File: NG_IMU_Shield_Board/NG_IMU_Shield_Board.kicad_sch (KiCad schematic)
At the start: 22 parts, among them J1 Conn_01x04_Female, J2 Conn_01x02_Male, J3 Conn_01x10_Female, J4 Conn_01x03_Female, J5 Conn_02x12_Top_Bottom, J6 Conn_01x11_Male, U1 SN75ALS175, U2 Level_Converter, U3 Teensy_v4.0

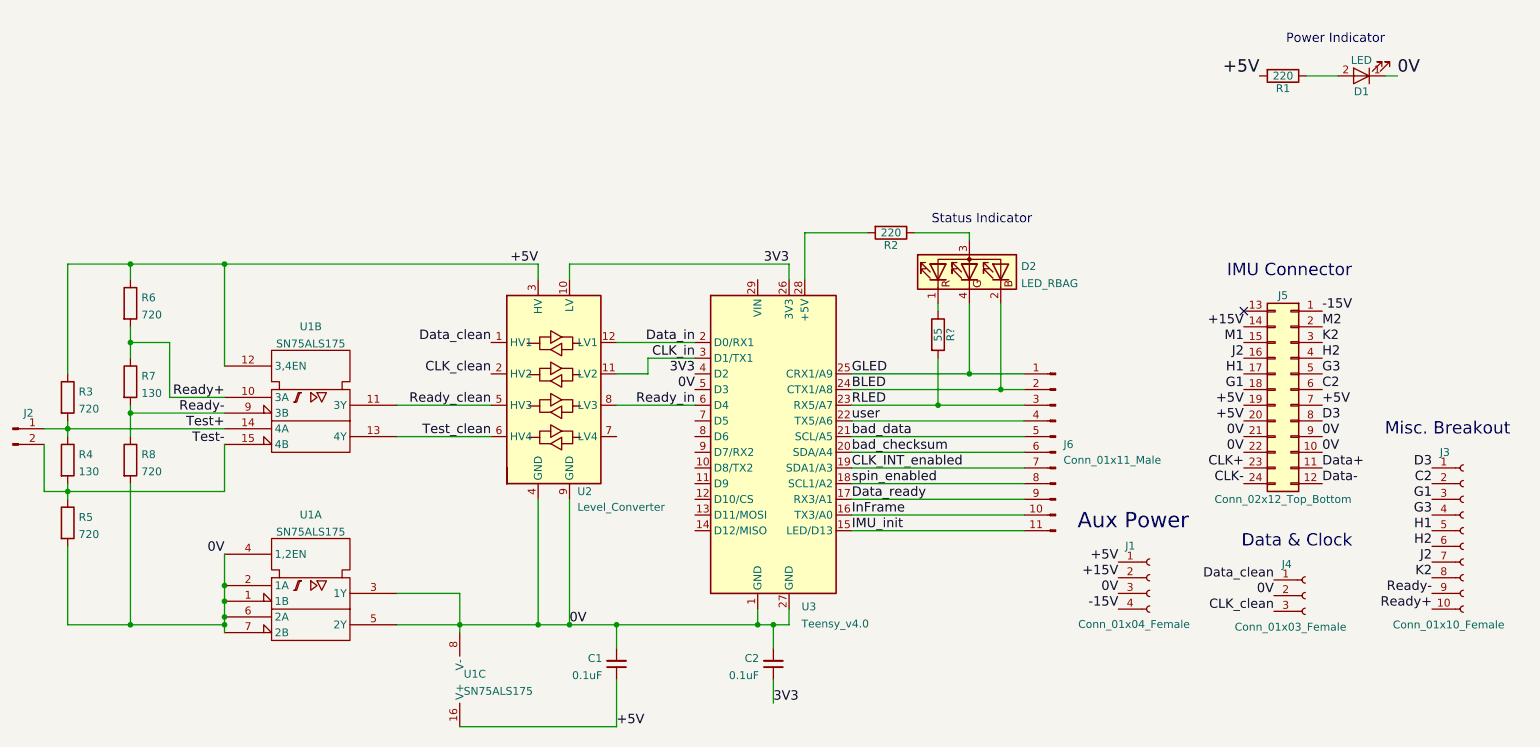
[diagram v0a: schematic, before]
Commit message: Simplified and updated footprints to ease routing
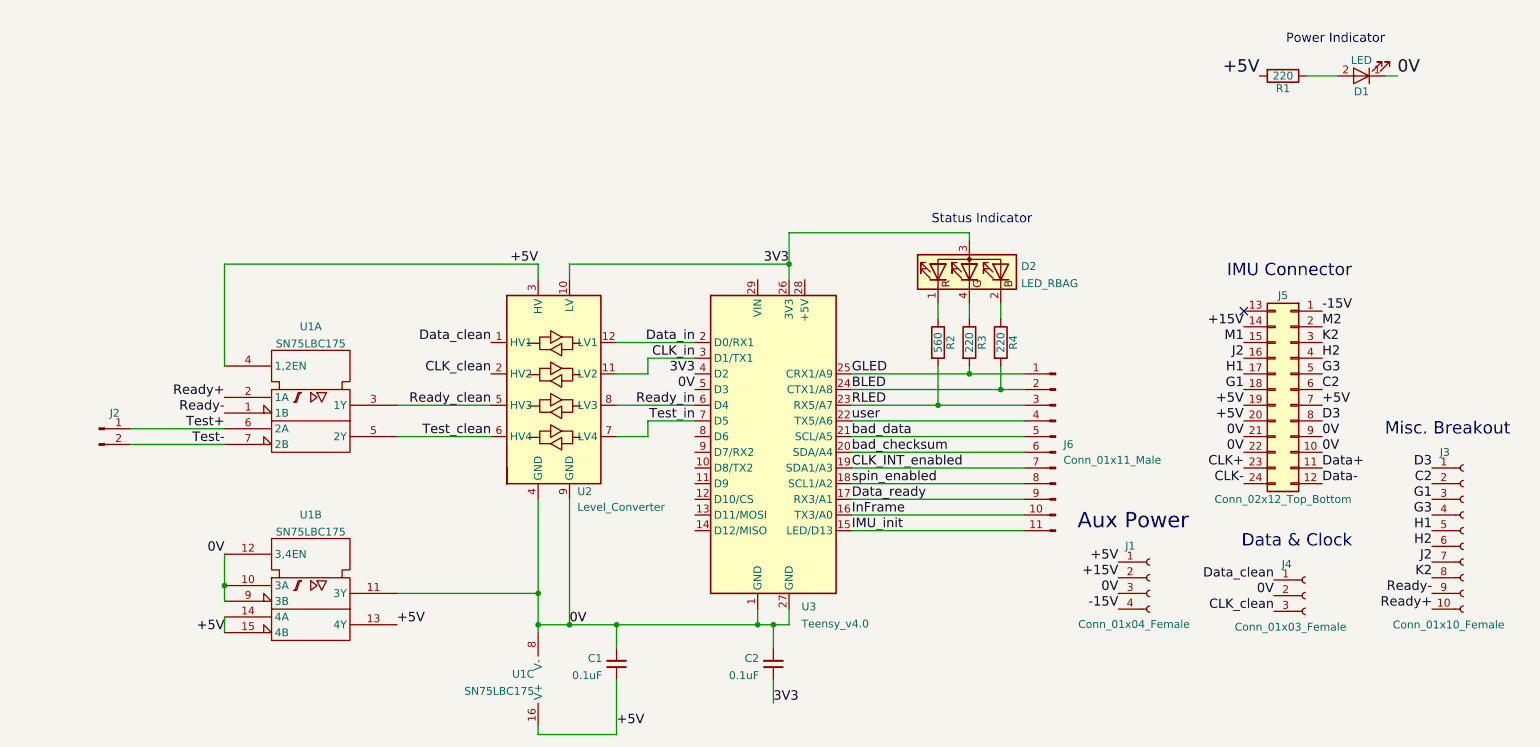
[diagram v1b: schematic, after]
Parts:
- removed R2: 220, Resistor_THT:R_Axial_DIN0204_L3.6mm_D1.6mm_P7.62mm_Horizontal, symbol NG_IMU_Interface_Board-rescue:R
- removed R3, R5, R6, R8: 720, Resistor_THT:R_Axial_DIN0204_L3.6mm_D1.6mm_P7.62mm_Horizontal, symbol Device:R
- removed R4, R7: 130, Resistor_THT:R_Axial_DIN0204_L3.6mm_D1.6mm_P7.62mm_Horizontal, symbol Device:R
- added R3, R4: 220, Resistor_SMD:R_0805_2012Metric_Pad1.20x1.40mm_HandSolder, symbol NG_IMU_Interface_Board-rescue:R
- R1: footprint Resistor_THT:R_Axial_DIN0204_L3.6mm_D1.6mm_P7.62mm_Horizontal -> Resistor_SMD:R_0805_2012Metric_Pad1.20x1.40mm_HandSolder
- R2: renamed from R?; value 55 -> 560; footprint Resistor_THT:R_Axial_DIN0204_L3.6mm_D1.6mm_P7.62mm_Horizontal -> Resistor_SMD:R_0805_2012Metric_Pad1.20x1.40mm_HandSolder
- U1: value SN75ALS175 -> SN75LBC175; footprint Package_DIP:DIP-16_W7.62mm_Socket -> Package_SO:SOIC-16_3.9x9.9mm_P1.27mm
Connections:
- net +5V: now also U1.13 (4Y), U1.14 (4A), U1.15 (4B), U1.4 (1,2EN); no longer U1.12 (3,4EN)
- net 0V: now also U1.10 (3A), U1.11 (3Y), U1.12 (3,4EN), U1.9 (3B); no longer U1.1 (1B), U1.2 (1A), U1.3 (1Y), U1.4 (1,2EN), U1.5 (2Y), U1.6 (2A), U1.7 (2B)
- net 3V3: now also D2.3 (A)
- net BLED: now also R4.2; no longer D2.2 (BK)
- net GLED: now also R3.2; no longer D2.4 (GK)
- net Ready+: now also U1.2 (1A); no longer U1.10 (3A)
- net Ready-: now also U1.1 (1B); no longer U1.9 (3B)
- net Ready_clean: now also U1.3 (1Y); no longer U1.11 (3Y)
- net Test+: now also U1.6 (2A); no longer U1.14 (4A)
- net Test-: now also U1.7 (2B); no longer U1.15 (4B)
- net Test_clean: now also U1.5 (2Y); no longer U1.13 (4Y)
- net Test_in: now reaches U3.7 (D5)
- net Test_in: now also U2.7 (LV4)
- new net: D2.2 (BK), R4.1
- new net: D2.4 (GK), R3.1
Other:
- moved on the sheet: J2, R2, U1A, U1B, U1C

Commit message: Finished routing board
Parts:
- added R5, R6: 120, Resistor_SMD:R_1206_3216Metric_Pad1.30x1.75mm_HandSolder, symbol NG_IMU_Interface_Board-rescue:R
- D2: value LED_RBAG -> LED_GABR; symbol Device:LED_RBAG -> Device:LED_GABR
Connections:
- net 3V3: now also D2.2 (A); no longer D2.3 (A)
- net Ready+: now also R5.2
- net Ready-: now also R5.1
- net Test+: now also R6.1
- net Test-: now also R6.2
- net at R4.1: now also D2.3 (BK); no longer D2.2 (BK)
- net at R3.1: now also D2.1 (GK); no longer D2.4 (GK)
- net at R2.1: now also D2.4 (RK); no longer D2.1 (RK)
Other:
- moved on the sheet: J2
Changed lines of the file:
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@@
   (junction (at 142.24 68.58) (diameter 0) (color 0 0 0 0)
+  )
+  (junction (at 38.1 105.41) (diameter 0) (color 0 0 0 0)
+  )
+  (junction (at 38.1 95.25) (diameter 0) (color 0 0 0 0)
   )
   (junction (at 114.3 127) (diameter 0) (color 0 0 0 0)
@@
     (stroke (width 0) (type default) (color 0 0 0 0))
   )
+  (wire (pts (xy 29.21 105.41) (xy 38.1 105.41))
+    (stroke (width 0) (type default) (color 0 0 0 0))
+  )
+  (wire (pts (xy 38.1 95.25) (xy 50.8 95.25))
+    (stroke (width 0) (type default) (color 0 0 0 0))
+  )
   (wire (pts (xy 78.74 96.52) (xy 93.98 96.52))
     (stroke (width 0) (type default) (color 0 0 0 0))
   )
+  (wire (pts (xy 29.21 97.79) (xy 29.21 105.41))
+    (stroke (width 0) (type default) (color 0 0 0 0))
+  )
+  (wire (pts (xy 22.86 97.79) (xy 29.21 97.79))
+    (stroke (width 0) (type default) (color 0 0 0 0))
+  )
   (wire (pts (xy 119.38 86.36) (xy 119.38 83.82))
     (stroke (width 0) (type default) (color 0 0 0 0))
   )
+  (wire (pts (xy 50.8 97.79) (xy 41.91 97.79))
+    (stroke (width 0) (type default) (color 0 0 0 0))
+  )
   (wire (pts (xy 226.06 38.1) (xy 231.14 38.1))
     (stroke (width 0) (type default) (color 0 0 0 0))
@@
     (stroke (width 0) (type default) (color 0 0 0 0))
   )
+  (wire (pts (xy 41.91 82.55) (xy 38.1 82.55))
+    (stroke (width 0) (type default) (color 0 0 0 0))
+  )
   (wire (pts (xy 139.7 127) (xy 142.24 127))
     (stroke (width 0) (type default) (color 0 0 0 0))
@@
     (stroke (width 0) (type default) (color 0 0 0 0))
   )
+  (wire (pts (xy 38.1 92.71) (xy 50.8 92.71))
+    (stroke (width 0) (type default) (color 0 0 0 0))
+  )
   (wire (pts (xy 101.6 144.78) (xy 101.6 143.51))
     (stroke (width 0) (type default) (color 0 0 0 0))
@@
     (stroke (width 0) (type default) (color 0 0 0 0))
   )
+  (wire (pts (xy 38.1 91.44) (xy 38.1 92.71))
+    (stroke (width 0) (type default) (color 0 0 0 0))
+  )
   (wire (pts (xy 176.53 74.93) (xy 176.53 77.47))
     (stroke (width 0) (type default) (color 0 0 0 0))
   )
+  (wire (pts (xy 38.1 82.55) (xy 38.1 83.82))
+    (stroke (width 0) (type default) (color 0 0 0 0))
+  )
   (wire (pts (xy 114.3 130.81) (xy 114.3 127))
     (stroke (width 0) (type default) (color 0 0 0 0))
@@
     (stroke (width 0) (type default) (color 0 0 0 0))
   )
+  (wire (pts (xy 38.1 105.41) (xy 38.1 104.14))
+    (stroke (width 0) (type default) (color 0 0 0 0))
+  )
   (wire (pts (xy 106.68 127) (xy 114.3 127))
     (stroke (width 0) (type default) (color 0 0 0 0))
@@
     (stroke (width 0) (type default) (color 0 0 0 0))
   )
-  (wire (pts (xy 35.56 95.25) (xy 50.8 95.25))
-    (stroke (width 0) (type default) (color 0 0 0 0))
-  )
   (wire (pts (xy 50.8 120.65) (xy 50.8 123.19))
     (stroke (width 0) (type default) (color 0 0 0 0))
@@
     (stroke (width 0) (type default) (color 0 0 0 0))
   )
+  (wire (pts (xy 38.1 96.52) (xy 38.1 95.25))
+    (stroke (width 0) (type default) (color 0 0 0 0))
+  )
   (wire (pts (xy 238.76 38.1) (xy 240.792 38.1))
     (stroke (width 0) (type default) (color 0 0 0 0))
@@
     (stroke (width 0) (type default) (color 0 0 0 0))
   )
+  (wire (pts (xy 41.91 90.17) (xy 41.91 82.55))
+    (stroke (width 0) (type default) (color 0 0 0 0))
+  )
   (wire (pts (xy 106.68 71.12) (xy 106.68 68.58))
     (stroke (width 0) (type default) (color 0 0 0 0))
@@
     (stroke (width 0) (type default) (color 0 0 0 0))
   )
+  (wire (pts (xy 41.91 97.79) (xy 41.91 105.41))
+    (stroke (width 0) (type default) (color 0 0 0 0))
+  )
   (wire (pts (xy 50.8 85.09) (xy 50.8 68.58))
     (stroke (width 0) (type default) (color 0 0 0 0))
   )
+  (wire (pts (xy 50.8 90.17) (xy 41.91 90.17))
+    (stroke (width 0) (type default) (color 0 0 0 0))
+  )
   (wire (pts (xy 152.4 104.14) (xy 180.34 104.14))
     (stroke (width 0) (type default) (color 0 0 0 0))
@@
     (stroke (width 0) (type default) (color 0 0 0 0))
   )
+  (wire (pts (xy 22.86 95.25) (xy 38.1 95.25))
+    (stroke (width 0) (type default) (color 0 0 0 0))
+  )
   (wire (pts (xy 50.8 125.73) (xy 50.8 128.27))
     (stroke (width 0) (type default) (color 0 0 0 0))
@@
     (stroke (width 0) (type default) (color 0 0 0 0))
   )
+  (wire (pts (xy 41.91 105.41) (xy 38.1 105.41))
+    (stroke (width 0) (type default) (color 0 0 0 0))
+  )
   (wire (pts (xy 166.37 74.93) (xy 166.37 77.47))
-    (stroke (width 0) (type default) (color 0 0 0 0))
-  )
-  (wire (pts (xy 50.8 97.79) (xy 35.56 97.79))
     (stroke (width 0) (type default) (color 0 0 0 0))
   )
@@
     (effects (font (size 1.524 1.524)) (justify right bottom))
   )
-  (label "Test+" (at 50.8 95.25 180)
-    (effects (font (size 1.524 1.524)) (justify right bottom))
+  (label "Test+" (at 22.86 95.25 0)
+    (effects (font (size 1.524 1.524)) (justify left bottom))
   )
   (label "CLK-" (at 215.9 104.14 180)
@@
     (effects (font (size 1.524 1.524)) (justify left bottom))
   )
-  (label "Test-" (at 50.8 97.79 180)
-    (effects (font (size 1.524 1.524)) (justify right bottom))
+  (label "Test-" (at 22.86 97.79 0)
+    (effects (font (size 1.524 1.524)) (justify left bottom))
   )
   (label "Data_clean" (at 220.775 119.7407 180)
@@
     (pin "2")
   )
-  (symbol (lib_id "Connector:Conn_01x02_Male") (at 30.48 95.25 0) (unit 1)
-    (in_bom yes) (on_board yes)
-    (property "Reference" "J2" (id 0) (at 33.02 92.71 0))
-    (property "Value" "Conn_01x02_Male" (id 1) (at 33.02 100.33 0)
-      (effects (font (size 1.27 1.27)) hide)
-    )
-    (property "Footprint" "Connector_PinHeader_2.54mm:PinHeader_1x02_P2.54mm_Vertical" (id 2) (at 30.48 95.25 0)
-      (effects (font (size 1.27 1.27)) hide)
-    )
-    (property "Datasheet" "~" (id 3) (at 30.48 95.25 0)
+  (symbol (lib_id "Connector:Conn_01x02_Male") (at 17.78 95.25 0) (unit 1)
+    (in_bom yes) (on_board yes)
+    (property "Reference" "J2" (id 0) (at 20.32 92.71 0))
+    (property "Value" "Conn_01x02_Male" (id 1) (at 20.32 100.33 0)
+      (effects (font (size 1.27 1.27)) hide)
+    )
+    (property "Footprint" "Connector_PinHeader_2.54mm:PinHeader_1x02_P2.54mm_Vertical" (id 2) (at 17.78 95.25 0)
+      (effects (font (size 1.27 1.27)) hide)
+    )
+    (property "Datasheet" "~" (id 3) (at 17.78 95.25 0)
+      (effects (font (size 1.27 1.27)) hide)
+    )
+    (pin "1")
+    (pin "2")
+  )
+  (symbol (lib_id "NG_IMU_Interface_Board-rescue:R") (at 38.1 100.33 0) (mirror y) (unit 1)
+    (in_bom yes) (on_board yes)
+    (property "Reference" "R6" (id 0) (at 36.068 100.33 90))
+    (property "Value" "120" (id 1) (at 38.1 100.33 90))
+    (property "Footprint" "Resistor_SMD:R_1206_3216Metric_Pad1.30x1.75mm_HandSolder" (id 2) (at 39.878 100.33 90)
+      (effects (font (size 1.27 1.27)) hide)
+    )
+    (property "Datasheet" "" (id 3) (at 38.1 100.33 0)
       (effects (font (size 1.27 1.27)) hide)
     )
@@
     (pin "3")
     (pin "4")
+  )
+  (symbol (lib_id "NG_IMU_Interface_Board-rescue:R") (at 38.1 87.63 180) (unit 1)
+    (in_bom yes) (on_board yes)
+    (property "Reference" "R5" (id 0) (at 36.068 87.63 90))
+    (property "Value" "120" (id 1) (at 38.1 87.63 90))
+    (property "Footprint" "Resistor_SMD:R_1206_3216Metric_Pad1.30x1.75mm_HandSolder" (id 2) (at 39.878 87.63 90)
+      (effects (font (size 1.27 1.27)) hide)
+    )
+    (property "Datasheet" "" (id 3) (at 38.1 87.63 0)
+      (effects (font (size 1.27 1.27)) hide)
+    )
+    (pin "1")
+    (pin "2")
   )
   (symbol (lib_id "NG_IMU_Shield_Board:SN75ALS175") (at 64.77 124.46 0) (unit 2)
@@
     (pin "8")
   )
-  (symbol (lib_id "Device:LED_RBAG") (at 171.45 69.85 90) (unit 1)
+  (symbol (lib_id "Device:LED_GABR") (at 171.45 69.85 90) (unit 1)
     (in_bom yes) (on_board yes) (fields_autoplaced)
     (property "Reference" "D2" (id 0) (at 179.832 68.9415 90)
       (effects (font (size 1.27 1.27)) (justify right))
     )
-    (property "Value" "LED_RBAG" (id 1) (at 179.832 71.7166 90)
+    (property "Value" "LED_GABR" (id 1) (at 179.832 71.7166 90)
       (effects (font (size 1.27 1.27)) (justify right))
     )
@@
     )
     (path "/9a55697f-0717-4220-8b7e-207e8d2e8edf"
-      (reference "D2") (unit 1) (value "LED_RBAG") (footprint "LED_THT:LED_D5.0mm-4_RGB")
+      (reference "D2") (unit 1) (value "LED_GABR") (footprint "LED_THT:LED_D5.0mm-4_RGB")
     )
     (path "/5f896468-93f7-4c01-b3ab-067ed3875a14"
@@
       (reference "R4") (unit 1) (value "220") (footprint "Resistor_SMD:R_0805_2012Metric_Pad1.20x1.40mm_HandSolder")
     )
+    (path "/6ac440ba-4881-4f79-8968-a3e9f9fd1b3e"
+      (reference "R5") (unit 1) (value "120") (footprint "Resistor_SMD:R_1206_3216Metric_Pad1.30x1.75mm_HandSolder")
+    )
+    (path "/53209e6b-2640-4435-b0ad-e5142285de26"
+      (reference "R6") (unit 1) (value "120") (footprint "Resistor_SMD:R_1206_3216Metric_Pad1.30x1.75mm_HandSolder")
+    )
     (path "/fbc7cd5b-7c4b-43fd-8ef9-d6da5696149d"

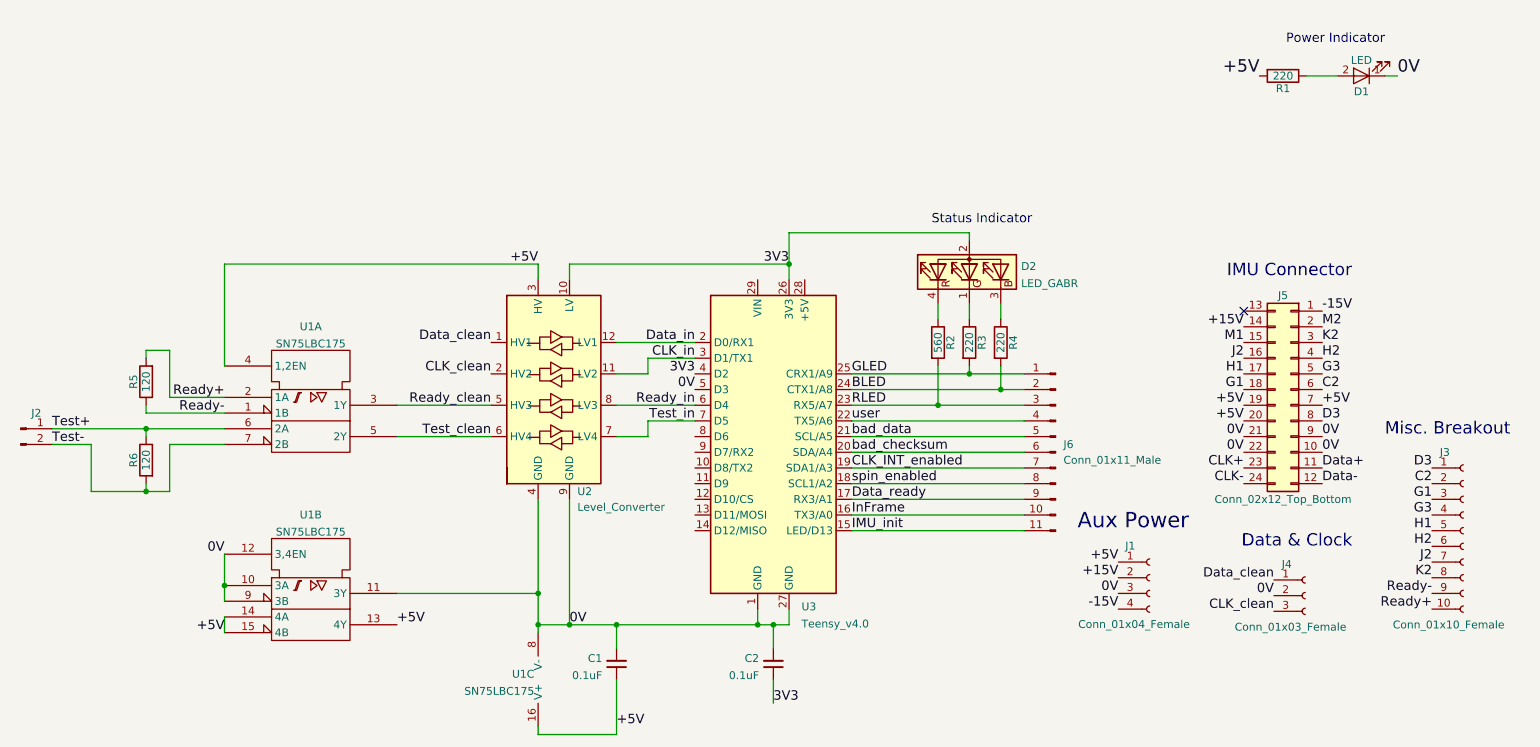
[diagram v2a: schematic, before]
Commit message: Moved status LED, added more user signals, other improvements
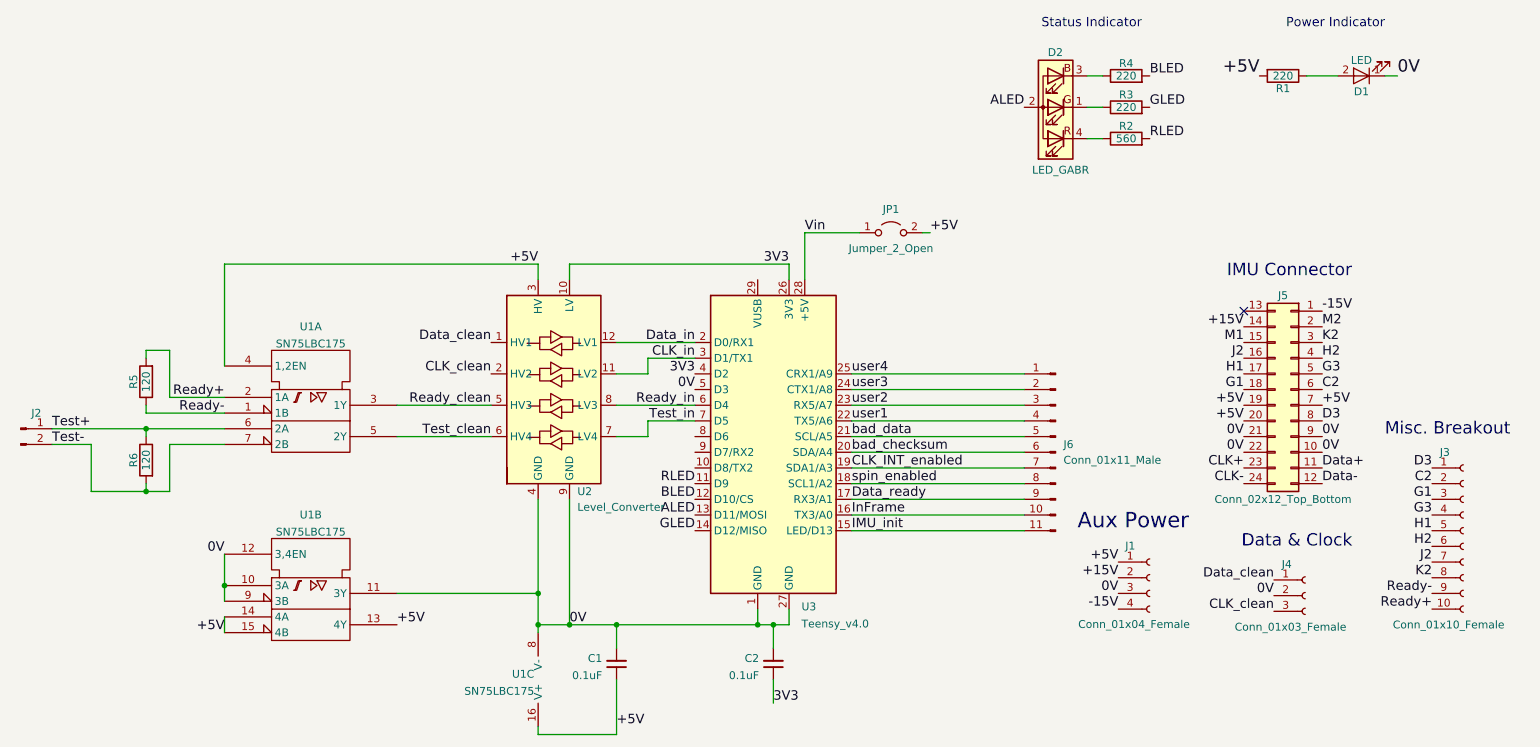
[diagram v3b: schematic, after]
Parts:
- added JP1: Jumper_2_Open, Connector_PinHeader_2.54mm:PinHeader_1x02_P2.54mm_Vertical, symbol Jumper:Jumper_2_Open
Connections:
- net +5V: now also JP1.2 (B)
- net 3V3: no longer D2.2 (A)
- net BLED: now also U3.12 (D10/CS); no longer J6.2 (Pin_2), U3.24 (CTX1/A8)
- net GLED: now also U3.14 (D12/MISO); no longer J6.1 (Pin_1), U3.25 (CRX1/A9)
- net RLED: now also U3.11 (D9); no longer J6.3 (Pin_3), U3.23 (RX5/A7)
- net ALED: now reaches U3.13 (D11/MOSI)
- net ALED: now also D2.2 (A)
- net Vin: now reaches U3.28 (+5V)
- net Vin: now also JP1.1 (A)
- net user renamed user1
- new net user2: J6.3 (Pin_3), U3.23 (RX5/A7)
- new net user3: J6.2 (Pin_2), U3.24 (CTX1/A8)
- new net user4: J6.1 (Pin_1), U3.25 (CRX1/A9)
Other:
- moved on the sheet: D2, R2, R3, R4
